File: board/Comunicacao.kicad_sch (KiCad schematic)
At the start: 1 part, among them U2 ESP32-WROOM-32

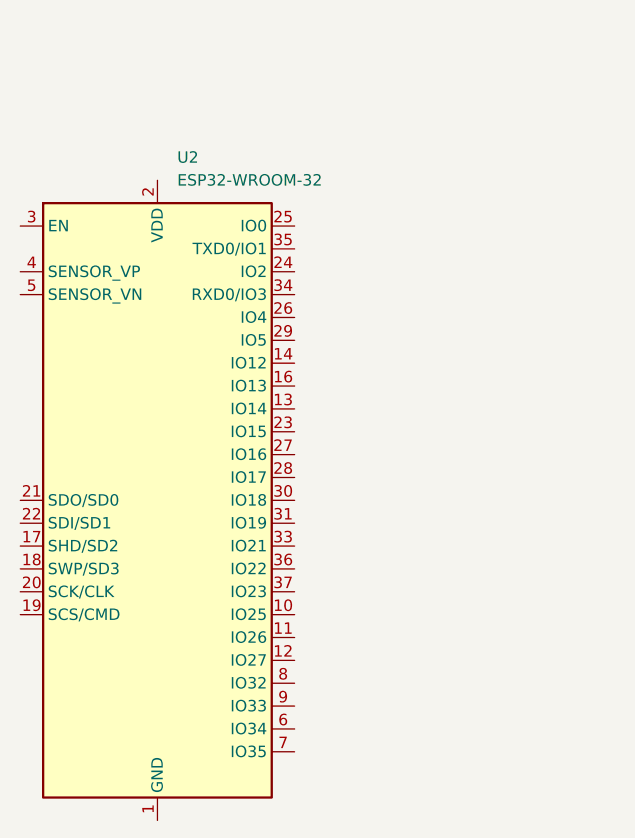
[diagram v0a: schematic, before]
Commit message: Schematic changes: correct micro board and subsystems
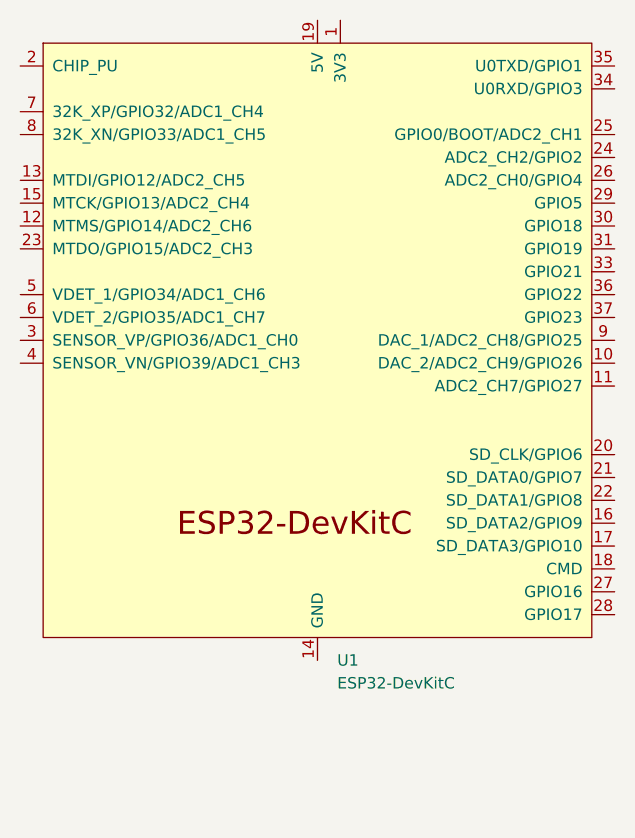
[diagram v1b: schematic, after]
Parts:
- removed U2: ESP32-WROOM-32, RF_Module:ESP32-WROOM-32, symbol RF_Module:ESP32-WROOM-32
- added U1: ESP32-DevKitC, PCM_Espressif:ESP32-DevKitC, symbol PCM_Espressif:ESP32-DevKitC
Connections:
- new net: U1.14 (GND), U1.32 (GND), U1.38 (GND)
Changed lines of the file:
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@@
 	(paper "A4")
 	(symbol
-		(lib_id "RF_Module:ESP32-WROOM-32")
-		(at 100.33 105.41 0)
+		(lib_id "PCM_Espressif:ESP32-DevKitC")
+		(at 118.11 87.63 0)
 		(unit 1)
 		(exclude_from_sim no)
@@
 		(dnp no)
 		(fields_autoplaced yes)
-		(property "Reference" "U2"
-			(at 102.5241 67.31 0)
+		(property "Reference" "U1"
+			(at 120.3041 123.19 0)
 			(effects
 				(font
@@
 			)
 		)
-		(property "Value" "ESP32-WROOM-32"
-			(at 102.5241 69.85 0)
+		(property "Value" "ESP32-DevKitC"
+			(at 120.3041 125.73 0)
 			(effects
 				(font
@@
 			)
 		)
-		(property "Footprint" "RF_Module:ESP32-WROOM-32"
-			(at 100.33 143.51 0)
+		(property "Footprint" "PCM_Espressif:ESP32-DevKitC"
+			(at 118.11 130.81 0)
 			(effects
 				(font
@@
 			)
 		)
-		(property "Datasheet" "https://www.espressif.com/sites/default/files/documentation/esp32-wroom-32_datasheet_en.pdf"
-			(at 92.71 104.14 0)
+		(property "Datasheet" "https://docs.espressif.com/projects/esp-idf/zh_CN/latest/esp32/hw-reference/esp32/get-started-devkitc.html"
+			(at 118.11 133.35 0)
 			(effects
 				(font
@@
 			)
 		)
-		(property "Description" "RF Module, ESP32-D0WDQ6 SoC, Wi-Fi 802.11b/g/n, Bluetooth, BLE, 32-bit, 2.7-3.6V, onboard antenna, SMD"
-			(at 100.33 105.41 0)
+		(property "Description" "Development Kit"
+			(at 118.11 87.63 0)
 			(effects
 				(font
@@
 			)
 		)
+		(pin "15"
+		)
+		(pin "12"
+		)
+		(pin "35"
+		)
+		(pin "32"
+		)
+		(pin "19"
+		)
+		(pin "1"
+		)
+		(pin "13"
+		)
+		(pin "34"
+		)
+		(pin "11"
+		)
+		(pin "17"
+		)
 		(pin "22"
+		)
+		(pin "4"
+		)
+		(pin "8"
+		)
+		(pin "31"
+		)
+		(pin "16"
+		)
+		(pin "10"
+		)
+		(pin "28"
+		)
+		(pin "5"
+		)
+		(pin "21"
 		)
 		(pin "2"
 		)
-		(pin "15"
+		(pin "9"
 		)
-		(pin "19"
-		)
-		(pin "32"
+		(pin "38"
 		)
 		(pin "20"
 		)
-		(pin "34"
+		(pin "14"
+		)
+		(pin "37"
+		)
+		(pin "7"
+		)
+		(pin "33"
+		)
+		(pin "18"
+		)
+		(pin "36"
+		)
+		(pin "27"
+		)
+		(pin "26"
+		)
+		(pin "25"
+		)
+		(pin "24"
+		)
+		(pin "30"
+		)
+		(pin "23"
 		)
 		(pin "3"
 		)
-		(pin "27"
-		)
-		(pin "35"
-		)
-		(pin "21"
-		)
-		(pin "12"
-		)
-		(pin "13"
-		)
-		(pin "16"
-		)
-		(pin "1"
-		)
-		(pin "10"
-		)
-		(pin "11"
-		)
-		(pin "26"
-		)
-		(pin "24"
-		)
-		(pin "9"
-		)
-		(pin "8"
+		(pin "29"
 		)
 		(pin "6"
-		)
-		(pin "31"
-		)
-		(pin "17"
-		)
-		(pin "23"
-		)
-		(pin "18"
-		)
-		(pin "25"
-		)
-		(pin "37"
-		)
-		(pin "36"
-		)
-		(pin "39"
-		)
-		(pin "28"
-		)
-		(pin "33"
-		)
-		(pin "7"
-		)
-		(pin "4"
-		)
-		(pin "29"
-		)
-		(pin "30"
-		)
-		(pin "14"
-		)
-		(pin "5"
-		)
-		(pin "38"
 		)
 		(instances
 			(project "board"
 				(path "/d7be55ed-3561-4de6-aa99-76e883d44fb9/92a0d1f9-4a95-4d63-a6fe-c77d28cfe3e8"
-					(reference "U2")
+					(reference "U1")
 					(unit 1)
 				)
